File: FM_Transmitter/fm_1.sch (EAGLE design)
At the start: 15 parts, among them T1 2N3904, T2 2N3904

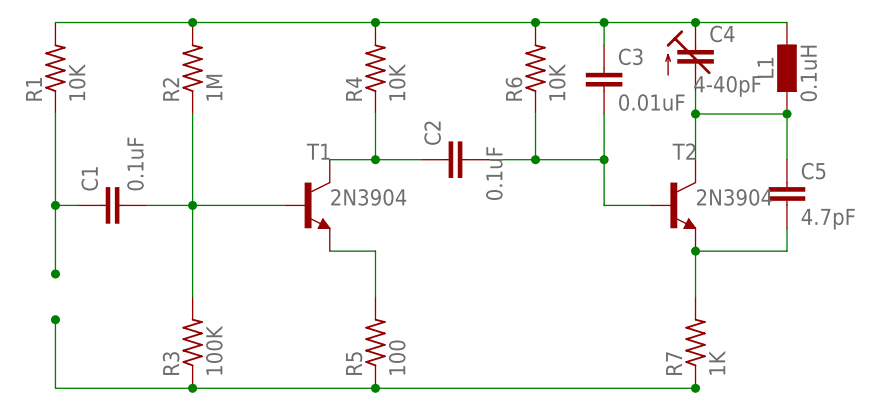
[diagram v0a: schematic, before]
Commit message: changed to 3pin Trimmer Cap + USN's corrected
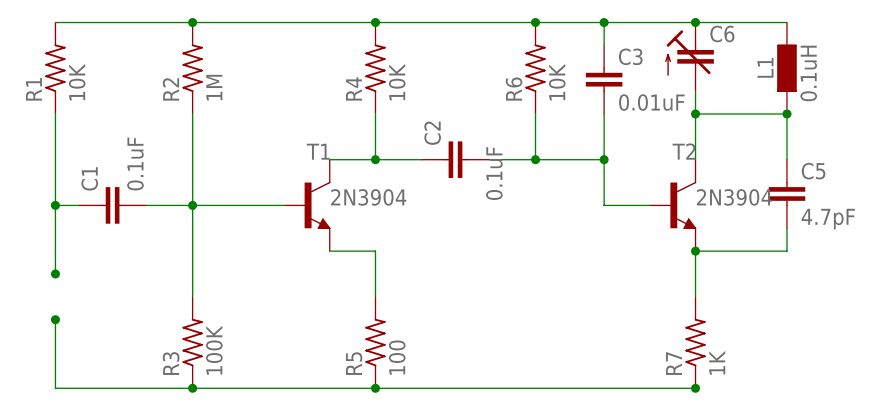
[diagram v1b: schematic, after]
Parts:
- removed C4: 4-40pF, rcl:C-TRIMM3050.505
- added C6: (no value), rcl:C-TRIMM808
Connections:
- net N$1: now also C6.E; no longer C4.E
- net N$7: now also C6.A; no longer C4.A
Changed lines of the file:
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@@
 <part name="C3" library="rcl" library_urn="urn:adsk.eagle:library:334" deviceset="C-EU" device="025-040X050" package3d_urn="urn:adsk.eagle:package:23634/1" value="0.01uF"/>
 <part name="C5" library="rcl" library_urn="urn:adsk.eagle:library:334" deviceset="C-EU" device="025-040X050" package3d_urn="urn:adsk.eagle:package:23634/1" value="4.7pF"/>
-<part name="C4" library="rcl" library_urn="urn:adsk.eagle:library:334" deviceset="C-TRIMM" device="3050.505" package3d_urn="urn:adsk.eagle:package:23773/1" value="4-40pF"/>
 <part name="L1" library="eagle-ltspice" library_urn="urn:adsk.eagle:library:217" deviceset="L" device="0204/7" package3d_urn="urn:adsk.eagle:package:13274/1" value="0.1uH"/>
+<part name="C6" library="rcl" library_urn="urn:adsk.eagle:library:334" deviceset="C-TRIMM" device="808" package3d_urn="urn:adsk.eagle:package:23766/1"/>
 </parts>
 <sheets>
@@
 <attribute name="VALUE" x="77.724" y="53.721" size="1.778" layer="96"/>
 </instance>
-<instance part="C4" gate="G$1" x="66.04" y="73.66" smashed="yes">
-<attribute name="NAME" x="67.564" y="74.041" size="1.778" layer="95"/>
-<attribute name="VALUE" x="65.786" y="68.453" size="1.778" layer="96"/>
-</instance>
 <instance part="L1" gate="G$1" x="76.2" y="71.12" smashed="yes">
 <attribute name="NAME" x="74.7014" y="69.85" size="1.778" layer="95" rot="R90"/>
 <attribute name="VALUE" x="79.502" y="67.31" size="1.778" layer="96" rot="R90"/>
+</instance>
+<instance part="C6" gate="G$1" x="66.04" y="73.66" smashed="yes">
+<attribute name="NAME" x="67.564" y="74.041" size="1.778" layer="95"/>
+<attribute name="VALUE" x="68.326" y="68.453" size="1.778" layer="96"/>
 </instance>
 </instances>
@@
 <segment>
 <pinref part="R1" gate="G$1" pin="2"/>
-<pinref part="C4" gate="G$1" pin="E"/>
 <wire x1="-5.08" y1="76.2" x2="10.16" y2="76.2" width="0.1524" layer="91"/>
 <wire x1="10.16" y1="76.2" x2="30.48" y2="76.2" width="0.1524" layer="91"/>
@@
 <pinref part="L1" gate="G$1" pin="1"/>
 <wire x1="55.88" y1="76.2" x2="66.04" y2="76.2" width="0.1524" layer="91"/>
-<wire x1="66.04" y1="76.2" x2="76.2" y2="76.2" width="0.1524" layer="91"/>
-<junction x="66.04" y="76.2"/>
 <pinref part="R2" gate="G$1" pin="2"/>
 <junction x="10.16" y="76.2"/>
@@
 <junction x="48.26" y="76.2"/>
 <pinref part="C3" gate="G$1" pin="1"/>
+<wire x1="66.04" y1="76.2" x2="76.2" y2="76.2" width="0.1524" layer="91"/>
 <wire x1="55.88" y1="73.66" x2="55.88" y2="76.2" width="0.1524" layer="91"/>
 <junction x="55.88" y="76.2"/>
+<pinref part="C6" gate="G$1" pin="E"/>
+<junction x="66.04" y="76.2"/>
 </segment>
 </net>
@@
 <net name="N$7" class="0">
 <segment>
-<pinref part="C4" gate="G$1" pin="A"/>
 <pinref part="T2" gate="G1" pin="C"/>
-<wire x1="66.04" y1="68.58" x2="66.04" y2="66.04" width="0.1524" layer="91"/>
 <pinref part="L1" gate="G$1" pin="2"/>
 <wire x1="66.04" y1="66.04" x2="66.04" y2="60.96" width="0.1524" layer="91"/>
@@
 <wire x1="76.2" y1="66.04" x2="76.2" y2="60.96" width="0.1524" layer="91"/>
 <junction x="76.2" y="66.04"/>
+<pinref part="C6" gate="G$1" pin="A"/>
+<wire x1="66.04" y1="68.58" x2="66.04" y2="66.04" width="0.1524" layer="91"/>
 </segment>
 </net>
